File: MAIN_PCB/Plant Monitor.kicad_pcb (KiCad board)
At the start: 6 copper layers, 42.8 x 66.3 mm, 59 parts, among them J1 TYPE-C-31-M-12, J2 Motor 1, J3 Motor 2, J4 Grove Connector for Soil Mois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, J5 Grove Connector for OLED Disp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, J6 Conn_01x14, J7 Conn_01x14, J8 JST PH-2Pin, J9 BME280 Terminals, Q1 AO3401A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

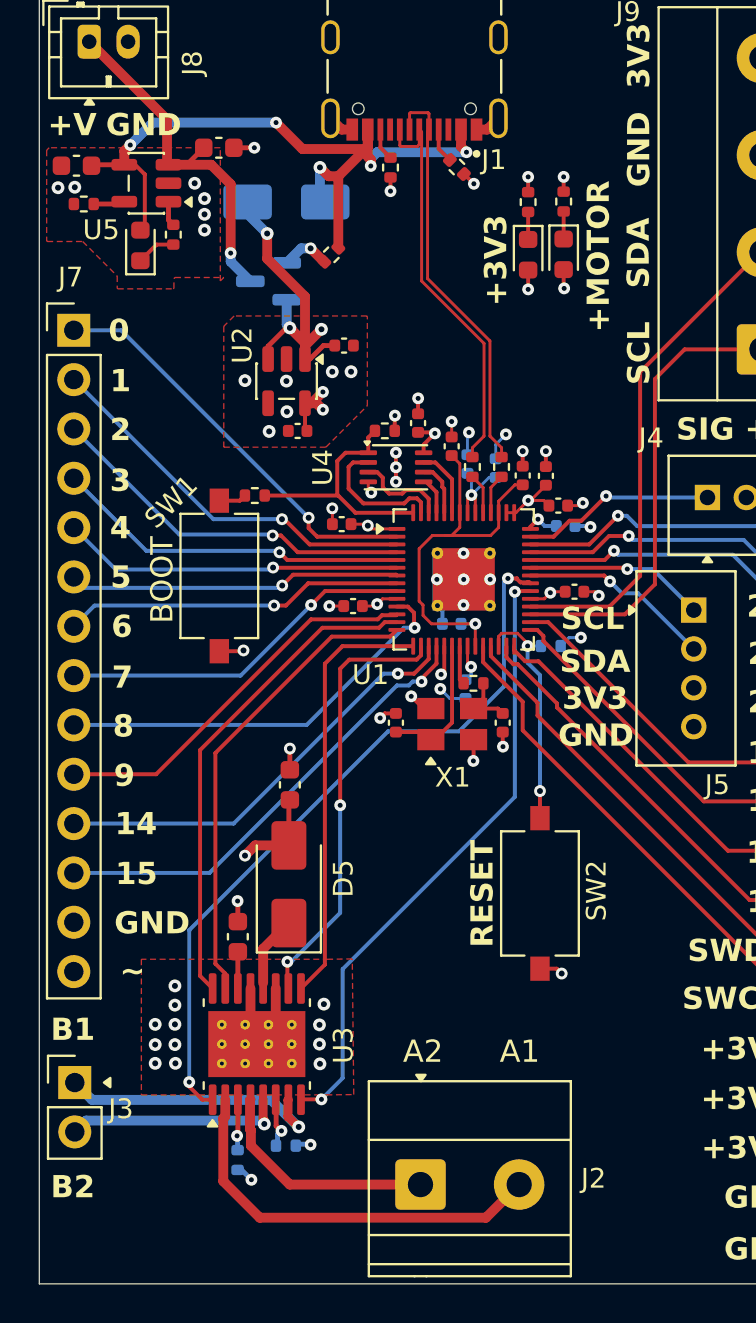
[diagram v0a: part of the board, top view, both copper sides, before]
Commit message: Finished README, added full BOM, deleted the unnecessary BME280 PCB files
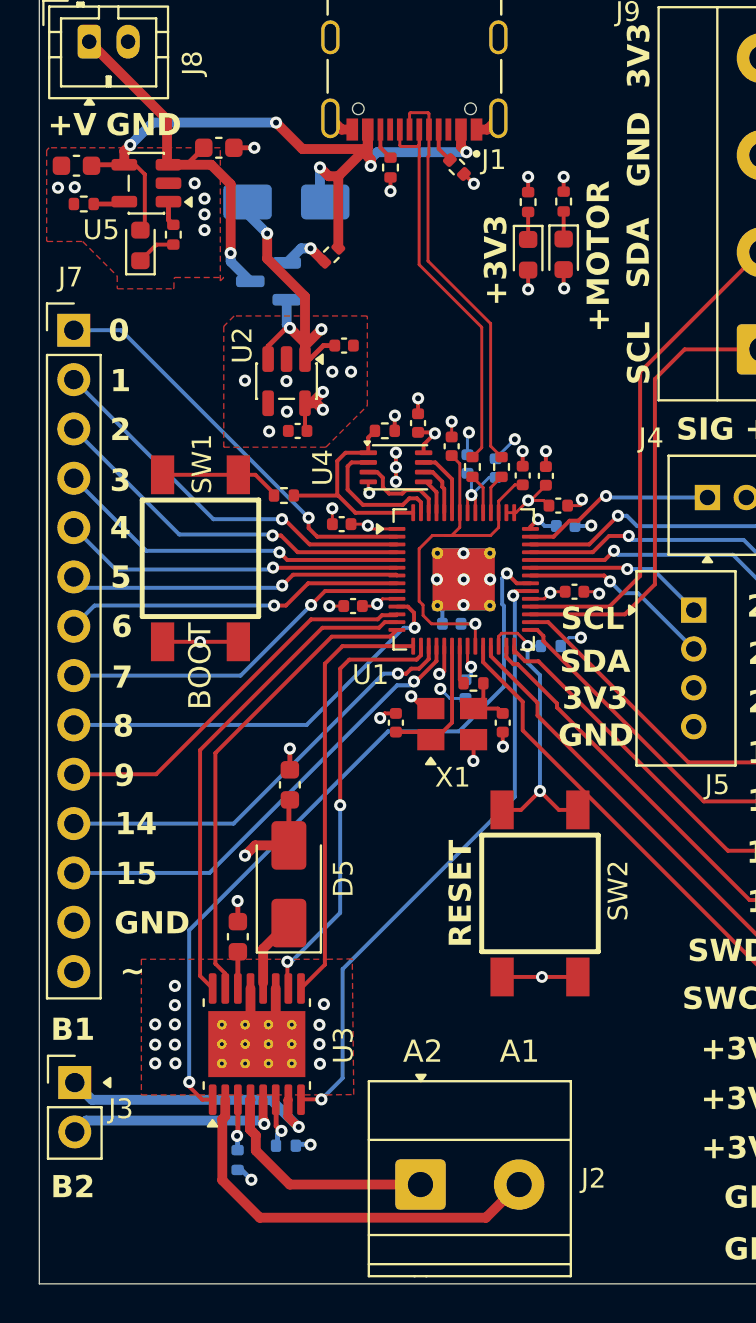
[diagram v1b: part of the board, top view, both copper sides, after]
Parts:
- moved R9 1.50 mm to (12.6, 25.7)
- moved SW1 1.33 mm to (8.33, 28.9)
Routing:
- net GND: track 34.4 -> 39.9 mm
- net Net-(R9-Pad1): track 1.43 -> 6.24 mm
- net /RUN: track 12.2 -> 15.5 mm
- net /QSPI_SS: track 12.9 -> 11.4 mm
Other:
- board text removed: "SW1"

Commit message: Revision D of PCB design
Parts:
- C10, C12, C13, U2: moved to B.Cu
- U4: footprint Package_SON:Winbond_USON-8-1EP_3x2mm_P0.5mm_EP0.2x1.6mm -> Package_SO:SOIC-8_5.3x5.3mm_P1.27mm
- moved R8 7.58 mm to (12.1, 17.4)
- moved C13 6.22 mm to (7.22, 21.2), turned to 0 degrees
- moved C12 5.51 mm to (10.3, 17.0)
- moved U2 5.11 mm to (7.79, 18.6)
- moved C18 4.96 mm to (19.7, 17.0)
- moved C10 4.62 mm to (22.0, 27.7), turned to 0 degrees
- moved U4 4.45 mm to (16.0, 20.5)
- moved R9 1.32 mm to (12.0, 24.6)
- moved SW2 0.69 mm to (25.1, 46.2)
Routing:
- net /+MOTORVOLTAGE: track 24.8 -> 15.6 mm, vias 5 -> 6
- net /QSPI_SD1: track 7.21 -> 14.3 mm
- net /QSPI_SD2: track 4.84 -> 10.8 mm
- net /QSPI_SS: track 11.4 -> 17.3 mm
- net /QSPI_SD3: track 3.54 -> 8.05 mm
- net /QSPI_SCLK: track 2.80 -> 6.46 mm
- net /QSPI_SD0: track 1.81 -> 4.55 mm
- net +1V1: track 20.5 -> 18.9 mm, vias 1 -> 2
- net GND: track 39.9 -> 41.2 mm, vias 61 -> 79
- net Net-(R9-Pad1): track 6.24 -> 5.11 mm
- net /GPIO0: track 21.4 -> 22.2 mm
- net +3V3: track 27.3 -> 28.0 mm, vias 13 -> 14
- added copper zone on B.Cu, net GND
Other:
- board text removed: "All vias that are in pads and have a total diameter of 24 mils and hole diameter 10 mils should be filled with epoxy and capped over (IPC-4761 Type VII via) All vias within copper pours should also be filled with epoxy for thermal conductivity"
